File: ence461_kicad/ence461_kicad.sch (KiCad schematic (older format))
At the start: 66 parts, among them J1 Conn_02x05_Odd_Even, Q1 Q_PMOS_GSD, U1 LMV324, U2 LMV324, U3 LMV324, U4 74HC3G14DP, U5 LMV321, U6 NCV7344D13R2GOSCT-ND, U7 TPS717DRV-WSON, U8 TPS71433DRVR, U9 MKE16Z32VLD4

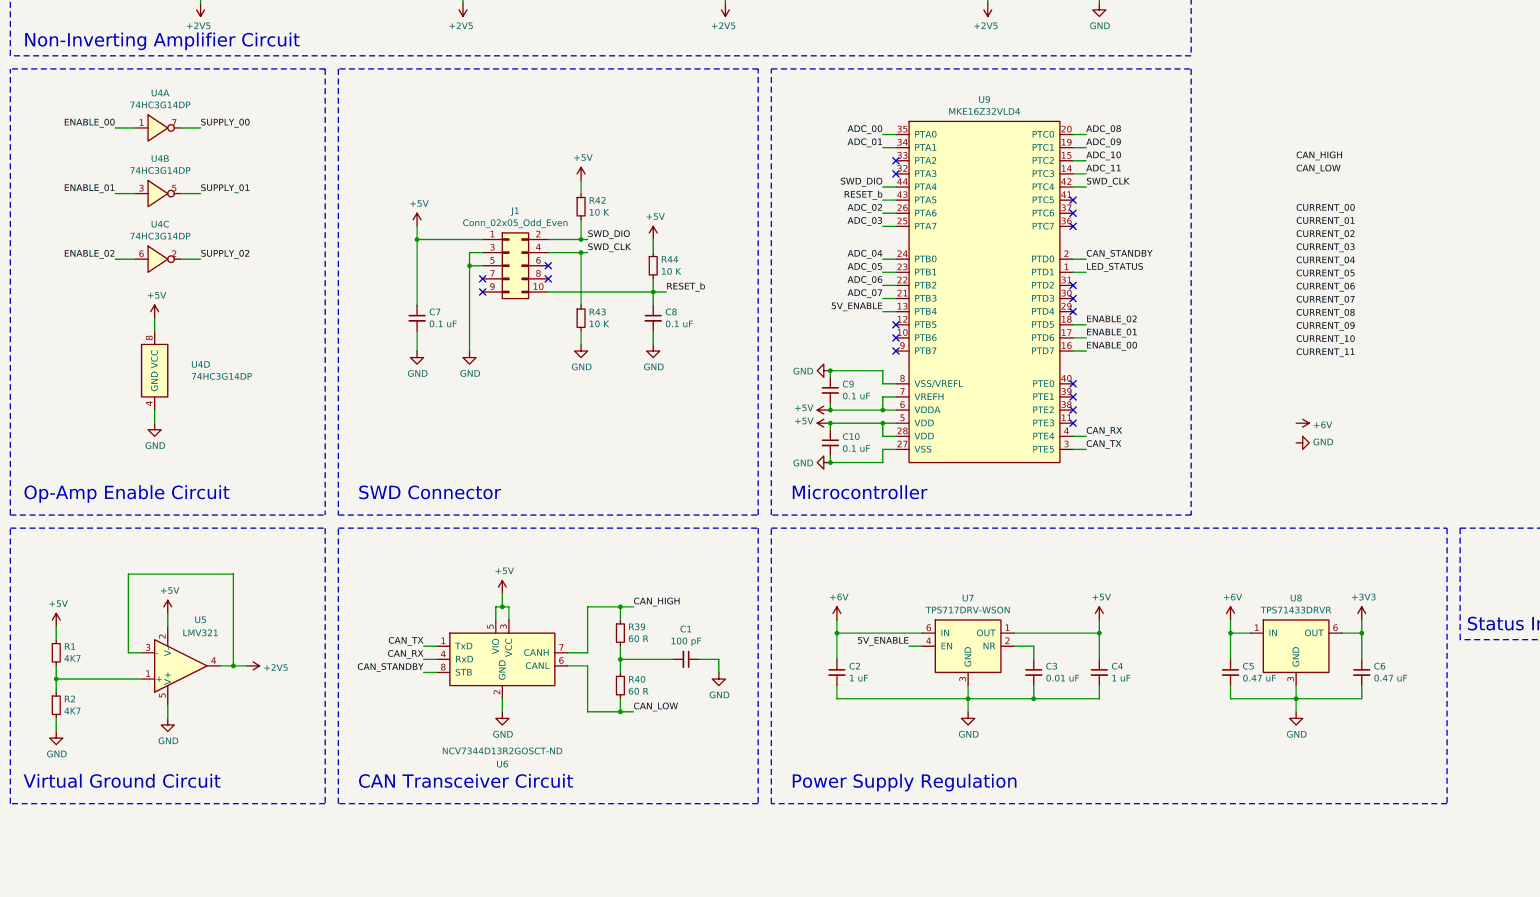
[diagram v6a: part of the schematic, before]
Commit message: Added symbol for new power supply to schematic.
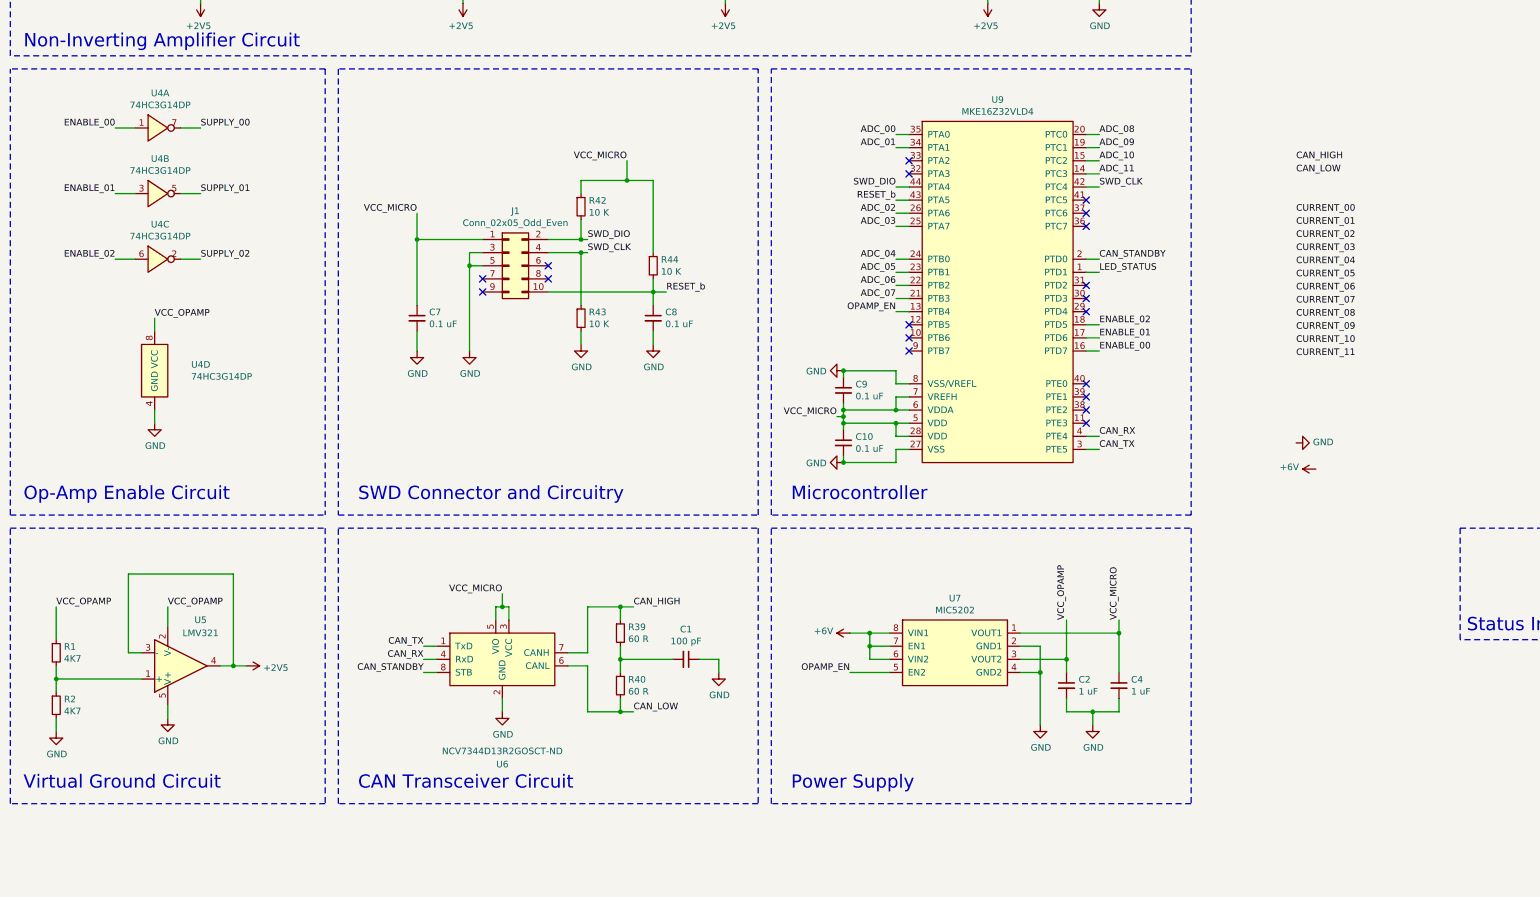
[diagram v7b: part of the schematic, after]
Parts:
- removed C3: 0.01 uF, Capacitor_SMD:C_0603_1608Metric, symbol Device:C_Small
- removed C5, C6: 0.47 uF, Capacitor_SMD:C_0603_1608Metric, symbol Device:C_Small
- removed U7: TPS717DRV-WSON, Package_SON:WSON-6-1EP_2x2mm_P0.65mm_EP1x1.6mm_ThermalVias, symbol ence461_symbol_library:TPS717DRV-WSON
- removed U8: TPS71433DRVR, Package_SON:WSON-6-1EP_2x2mm_P0.65mm_EP1x1.6mm, symbol ence461_symbol_library:TPS71433DRVR
- added U7: MIC5202, Package_SO:SOIC-8_3.9x4.9mm_P1.27mm, symbol ence461_symbol_library:MIC5202
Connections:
- net +6V: now also U7.6 (VIN2), U7.7 (EN1), U7.8 (VIN1); no longer C2.1
- net GND: now also U7.2 (GND1), U7.4 (GND2)
- net +5V renamed VCC_MICRO
- net VCC_MICRO: now also U7.1 (VOUT1); no longer R1.1, U4.8 (VCC), U5.2 (V-)
- net 5V_ENABLE renamed OPAMP_EN
- net OPAMP_EN: now also U7.5 (EN2)
- new net VCC_OPAMP: C2.1, R1.1, U4.8 (VCC), U5.2 (V-), U7.3 (VOUT2)
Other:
- note added: "Power Supply"
- note added: "SWD Connector and Circuitry"
- note removed: "Power Supply Regulation"
- note removed: "SWD Connector"
- moved on the sheet: C10, C2, C4, C9, U9

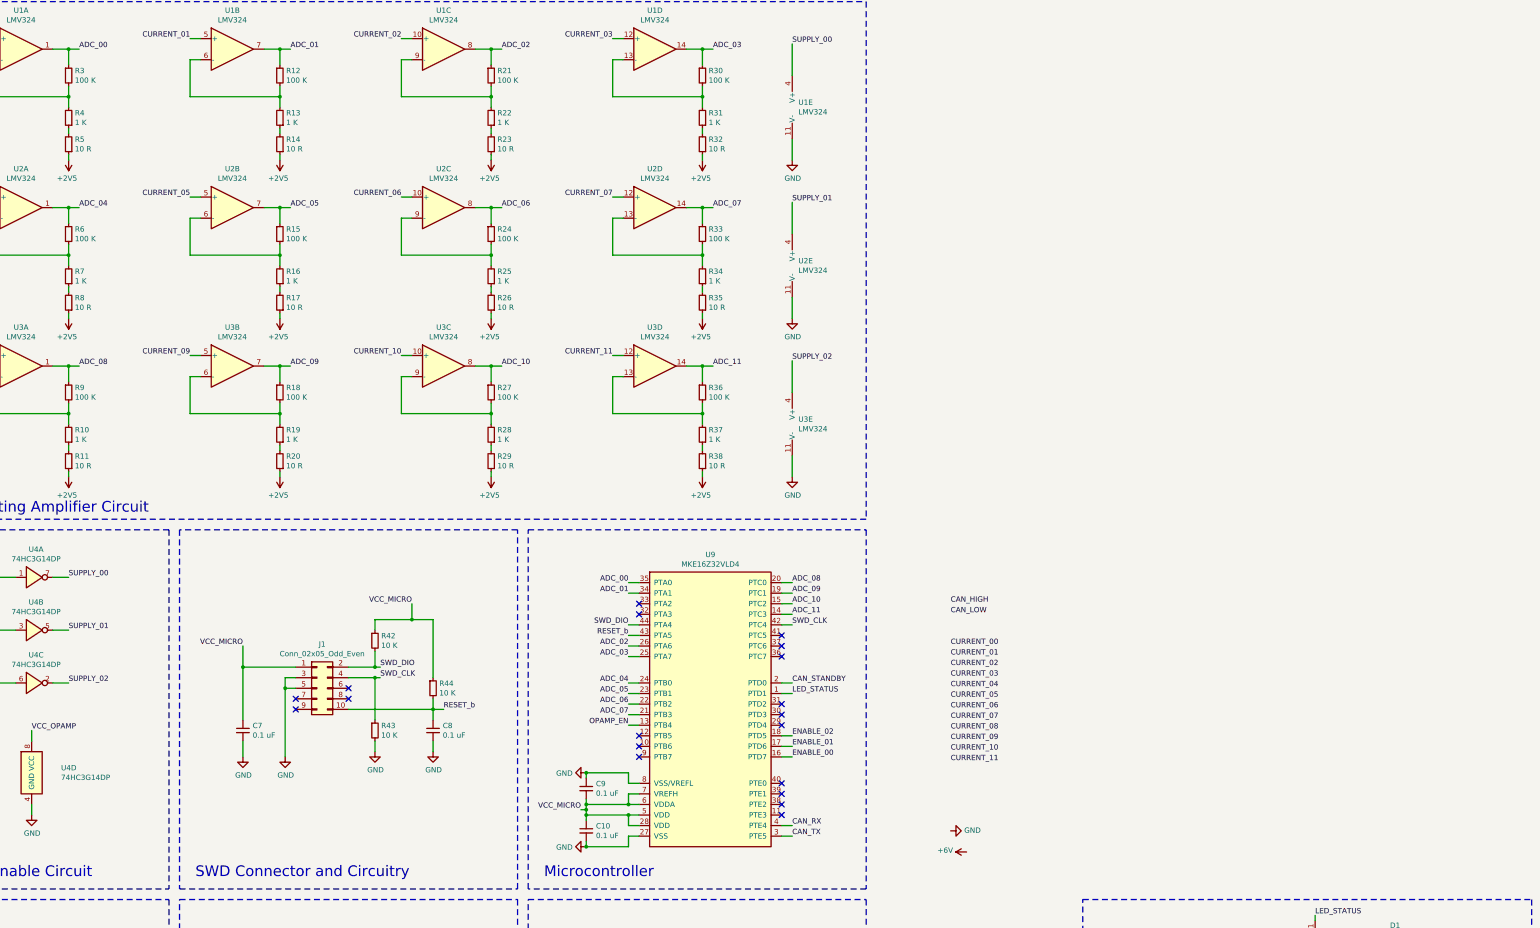
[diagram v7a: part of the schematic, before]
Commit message: Changed amplifier gain to 141
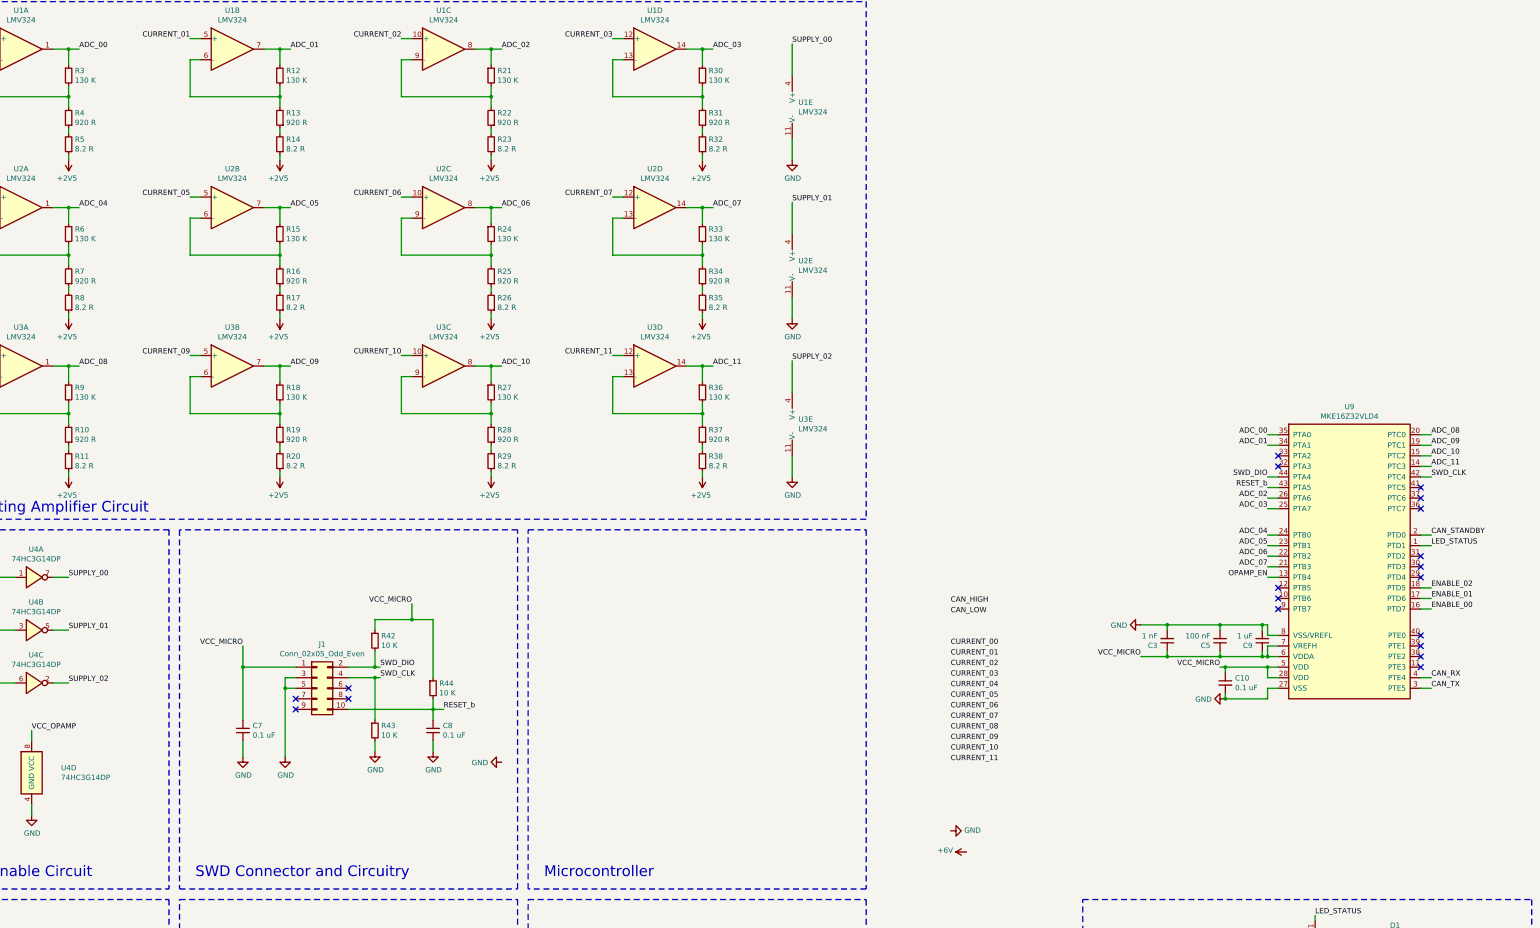
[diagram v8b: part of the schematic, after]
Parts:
- added C3: 1 nF, Capacitor_SMD:C_0603_1608Metric, symbol Device:C_Small
- added C5: 100 nF, Capacitor_SMD:C_0603_1608Metric, symbol Device:C_Small
- C9: value 0.1 uF -> 1 uF
- R10, R13, R16, R19, R22, R25, R28, R31, R34, R37, R4, R7: value 1 K -> 920 R
- R11, R14, R17, R20, R23, R26, R29, R32, R35, R38, R5, R8: value 10 R -> 8.2 R
- R12, R15, R18, R21, R24, R27, R3, R30, R33, R36, R6, R9: value 100 K -> 130 K
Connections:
- net GND: now also C9.2, C3.2, C5.2; no longer C9.1
- net VCC_MICRO: now also C9.1, C3.1, C5.1; no longer C9.2
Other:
- moved on the sheet: C10, C9, U9
